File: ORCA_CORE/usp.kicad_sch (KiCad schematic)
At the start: 15 parts, among them U11 AP64502

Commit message: made usp (sketch only)
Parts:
- added C29: 0.01u, symbol Device:C
- added C30, C34, C35: 0.1u, symbol Device:C
- added C31, C32, C36, C37, C38, C41, C42, C43: 4.7u, symbol Device:C
- added C33: 1u, symbol Device:C
- added D15: LED_batt_enabled, symbol Device:LED_Filled
- added D16, D17, D18: CUHS20560, symbol Device:D_Schottky
- added L1: L, symbol Device:L
- added Q5: PMOS, symbol Simulation_SPICE:PMOS
- added R23, R24: 100k, symbol Device:R
- added R25: 47k, symbol Device:R
- added R26: 4.7k, symbol Device:R
- added R27: 510, symbol Device:R
- added R28, R32, R33: 10k, symbol Device:R
- added R29: 2k, symbol Device:R
- added R30: 100, symbol Device:R
- added R31: 1k, symbol Device:R
- added U12: TPS61230A__board, symbol mylib:TPS61230A_board
- U10: value ~ -> HY2112
- U9: value ~ -> FS8205
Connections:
- net GND: now also U11.7 (GND), U11.9 (PAD), U9.3, C29.2, C31.1, C32.1, C33.1, C34.1, C36.1, C37.1, C38.1, C41.1, C42.1, C43.1, D15.1 (K), R24.2, R28.2, R29.2, R32.2, U12.3 (GND), U12.5 (GND)
- net VDD: now also C24.1, R22.1, U3.4 (VIN), D17.2 (A), R32.1, R33.2; no longer U11.2 (Vin), U11.3 (EN)
- net bat+: now reaches C25.1, U3.5 (BAT), U3.8 (FB)
- net at U10.1 (OD): now also U9.6
- net at U10.2 (CS): now also R29.1
- net at U10.3 (OC): now also U9.4
- net at U10.5 (VDD): now also C35.1, R30.1
- net batt-: now reaches U10.6 (VSS)
- net batt-: now also U9.1, C35.2
- net at U11.1 (BST): now also C30.2
- net at U11.4 (RT/CLK): now also R23.1
- net at U11.5 (FB): now also R27.2, R28.1
- net at U11.6 (SS): now also C29.1
- net at U11.8 (SW): now also C30.1, L1.1
- new net: Q5.2 (G), R33.1
- new net: R23.2, R24.1
- new net: D15.2 (A), R31.2
- new net: R25.1, R26.1
- new net: R26.2, R27.1
- new net Vout: C31.2, C32.2, C33.2, C34.2, D16.1 (K), D18.1 (K)
- new net batt+: Q5.1 (D), R30.2
- new net reg_down: D17.1 (K), U11.2 (Vin), U11.3 (EN)
- new net reg_down_out: D18.2 (A), L1.2, R25.2
- new net reg_up: C36.2, C37.2, C38.2, Q5.3 (S), R31.1, U12.1 (VIN), U12.2 (EN)
- new net reg_up_out: C41.2, C42.2, C43.2, D16.2 (A), U12.4 (VOUT)
- no-connect marks 0 -> 3
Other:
- note added: "3.3V -> 5V2.5A DCDC"
- note added: "9V -> 5V3A DCDC"
- note added: "battery protection"
- note added: "charger"
- note added: "load sharing system"
- note added: "power"
- moved on the sheet: C24, C25, C26, C27, C28, D10, D12, D13, F2, R21, R22, U10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

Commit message: made all sketch for test (cpu board is only for test
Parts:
- removed F2: Polyfuse, symbol Device:Polyfuse
- added C39: 1000u, symbol Device:C_Polarized
- added F2: Fuse, symbol Device:Fuse
- D13: value D_Schottky -> CUHS20560
- L1: value L -> 10u
- Q5: value PMOS -> TJ60S04M3L
- U3: value ~ -> CN3058E
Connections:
- net GND: now also C39.1
- net Vin: now also F2.2
- net Vout: now also C39.2
- net VDD renamed VDD_usp
- net VDD_usp: now also F2.1; no longer D17.2 (A), R32.1, R33.2
- new net +VDD_power: D17.2 (A), R32.1, R33.2

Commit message: attach all capacitors
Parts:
- C24, C27, C33: footprint (none) -> Capacitor_SMD:C_0805_2012Metric_Pad1.18x1.45mm_HandSolder
- C25: footprint (none) -> Capacitor_SMD:C_1206_3216Metric_Pad1.33x1.80mm_HandSolder
- C26, C28, C30, C31, C32, C34, C35, C36, C37, C38, C41, C42, C43: footprint (none) -> Capacitor_SMD:C_0603_1608Metric_Pad1.08x0.95mm_HandSolder
- D10, D12, D15: footprint (none) -> LED_SMD:LED_0603_1608Metric_Pad1.05x0.95mm_HandSolder
- D13, D16, D17, D18: footprint (none) -> Diode:Diode_US2H
- L1: footprint (none) -> Inductor_SMD:L_12x12mm_H8mm
- Q5: footprint (none) -> toshiba:2-7M1A
- R21, R22, R23, R24, R25, R26, R27, R28, R29, R30, R31, R32, R33: footprint (none) -> Resistor_SMD:R_0603_1608Metric_Pad0.98x0.95mm_HandSolder

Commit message: attach all the footprints
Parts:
- C29: footprint (none) -> Capacitor_SMD:C_0603_1608Metric_Pad1.08x0.95mm_HandSolder
- C39: footprint (none) -> Capacitor_THT:CP_Radial_D10.0mm_P5.00mm
- U10, U9: footprint (none) -> Package_TO_SOT_SMD:TSOT-23-6_HandSoldering
- U12: footprint (none) -> Converter_DCDC:TPS61230A
- U3: footprint (none) -> Package_SO:TSSOP-8_3x3mm_P0.65mm
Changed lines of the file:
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@@
       (effects (font (size 1.27 1.27)))
     )
-    (property "Footprint" "" (at 69.85 99.06 0)
+    (property "Footprint" "Package_SO:TSSOP-8_3x3mm_P0.65mm" (at 69.85 99.06 0)
       (effects (font (size 1.27 1.27)) hide)
     )
@@
       (effects (font (size 1.27 1.27)))
     )
-    (property "Footprint" "" (at 195.58 87.63 0)
+    (property "Footprint" "Package_TO_SOT_SMD:TSOT-23-6_HandSoldering" (at 195.58 87.63 0)
       (effects (font (size 1.27 1.27)) hide)
     )
@@
       (effects (font (size 1.27 1.27)) (justify left))
     )
-    (property "Footprint" "" (at 116.5352 49.53 0)
+    (property "Footprint" "Capacitor_SMD:C_0603_1608Metric_Pad1.08x0.95mm_HandSolder" (at 116.5352 49.53 0)
       (effects (font (size 1.27 1.27)) hide)
     )
@@
       (effects (font (size 1.27 1.27)))
     )
-    (property "Footprint" "" (at 195.58 101.6 0)
+    (property "Footprint" "Package_TO_SOT_SMD:TSOT-23-6_HandSoldering" (at 195.58 101.6 0)
       (effects (font (size 1.27 1.27)) hide)
     )
@@
       (effects (font (size 1.27 1.27)) (justify left))
     )
-    (property "Footprint" "" (at 153.3652 152.4 0)
+    (property "Footprint" "Capacitor_THT:CP_Radial_D10.0mm_P5.00mm" (at 153.3652 152.4 0)
       (effects (font (size 1.27 1.27)) hide)
     )
@@
       (effects (font (size 1.27 1.27)))
     )
-    (property "Footprint" "" (at 246.38 34.29 0)
-      (effects (font (size 1.27 1.27)) hide)
-    )
+    (property "Footprint" "Converter_DCDC:TPS61230A" (at 246.38 34.29 0)
+      (effects (font (size 1.27 1.27)) hide)
+    )

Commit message: change sketch a little
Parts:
- F2: footprint (none) -> fuse:fuse
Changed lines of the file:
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@@
       (effects (font (size 1.27 1.27)))
     )
-    (property "Footprint" "" (at 35.56 28.702 90)
+    (property "Footprint" "fuse:fuse" (at 35.56 28.702 90)
       (effects (font (size 1.27 1.27)) hide)
     )

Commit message: plate power
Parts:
- added H5, H6, H7, H8: Hole_usp, MountingHole:MountingHole_3.2mm_M3, symbol Mechanical:MountingHole
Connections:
- net VDD_usp is gone; now on net +VDD_usp: C24.1, C26.2, C27.2, C28.2, D13.1 (K), F2.1, R22.1, U3.4 (VIN)
- net +VDD_power renamed +VDD_usp
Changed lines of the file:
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@@
     )
   )
-  (global_label "+VDD_power" (shape input) (at 35.56 171.45 180) (fields_autoplaced)
+  (global_label "+VDD_usp" (shape input) (at 35.56 171.45 180) (fields_autoplaced)
     (effects (font (size 1.27 1.27)) (justify right))
-    (property "Intersheetrefs" "${INTERSHEET_REFS}" (at 20.9029 171.45 0)
+    (property "Intersheetrefs" "${INTERSHEET_REFS}" (at 23.0801 171.45 0)
       (effects (font (size 1.27 1.27)) (justify right) hide)
     )
@@
     )
   )
-  (global_label "VDD_usp" (shape input) (at 190.5 168.91 180) (fields_autoplaced)
+  (global_label "+VDD_usp" (shape input) (at 190.5 168.91 180) (fields_autoplaced)
     (effects (font (size 1.27 1.27)) (justify right))
-    (property "Intersheetrefs" "${INTERSHEET_REFS}" (at 179.5925 168.91 0)
+    (property "Intersheetrefs" "${INTERSHEET_REFS}" (at 178.0201 168.91 0)
       (effects (font (size 1.27 1.27)) (justify right) hide)
     )
@@
     )
   )
-  (global_label "VDD_usp" (shape input) (at 73.66 30.48 0) (fields_autoplaced)
+  (global_label "+VDD_usp" (shape input) (at 73.66 30.48 0) (fields_autoplaced)
     (effects (font (size 1.27 1.27)) (justify left))
-    (property "Intersheetrefs" "${INTERSHEET_REFS}" (at 84.5675 30.48 0)
+    (property "Intersheetrefs" "${INTERSHEET_REFS}" (at 86.1399 30.48 0)
       (effects (font (size 1.27 1.27)) (justify left) hide)
     )
@@
     )
   )
-  (global_label "VDD_usp" (shape input) (at 46.99 74.93 180) (fields_autoplaced)
+  (global_label "+VDD_usp" (shape input) (at 46.99 74.93 180) (fields_autoplaced)
     (effects (font (size 1.27 1.27)) (justify right))
-    (property "Intersheetrefs" "${INTERSHEET_REFS}" (at 36.0825 74.93 0)
+    (property "Intersheetrefs" "${INTERSHEET_REFS}" (at 34.5101 74.93 0)
       (effects (font (size 1.27 1.27)) (justify right) hide)
     )
@@
         (path "/895d6bb7-4008-488b-a34b-0077e9f7e4a1/6a7faaf2-e424-4dfa-bbc5-1df218d33dea"
           (reference "#PWR062") (unit 1)
+        )
+      )
+    )
+  )
+  (symbol (lib_id "Mechanical:MountingHole") (at 246.38 177.8 0) (unit 1)
+    (in_bom yes) (on_board yes) (dnp no) (fields_autoplaced)
+    (property "Reference" "H6" (at 248.92 176.53 0)
+      (effects (font (size 1.27 1.27)) (justify left))
+    )
+    (property "Value" "Hole_usp" (at 248.92 179.07 0)
+      (effects (font (size 1.27 1.27)) (justify left))
+    )
+    (property "Footprint" "MountingHole:MountingHole_3.2mm_M3" (at 246.38 177.8 0)
+      (effects (font (size 1.27 1.27)) hide)
+    )
+    (property "Datasheet" "~" (at 246.38 177.8 0)
+      (effects (font (size 1.27 1.27)) hide)
+    )
+    (instances
+      (project "ORCA_CORE"
+        (path "/895d6bb7-4008-488b-a34b-0077e9f7e4a1/6a7faaf2-e424-4dfa-bbc5-1df218d33dea"
+          (reference "H6") (unit 1)
         )
       )
@@
     )
   )
+  (symbol (lib_id "Mechanical:MountingHole") (at 264.16 170.18 0) (unit 1)
+    (in_bom yes) (on_board yes) (dnp no) (fields_autoplaced)
+    (property "Reference" "H7" (at 266.7 168.91 0)
+      (effects (font (size 1.27 1.27)) (justify left))
+    )
+    (property "Value" "Hole_usp" (at 266.7 171.45 0)
+      (effects (font (size 1.27 1.27)) (justify left))
+    )
+    (property "Footprint" "MountingHole:MountingHole_3.2mm_M3" (at 264.16 170.18 0)
+      (effects (font (size 1.27 1.27)) hide)
+    )
+    (property "Datasheet" "~" (at 264.16 170.18 0)
+      (effects (font (size 1.27 1.27)) hide)
+    )
+    (instances
+      (project "ORCA_CORE"
+        (path "/895d6bb7-4008-488b-a34b-0077e9f7e4a1/6a7faaf2-e424-4dfa-bbc5-1df218d33dea"
+          (reference "H7") (unit 1)
+        )
+      )
+    )
+  )
   (symbol (lib_id "Device:D_Schottky") (at 105.41 152.4 180) (unit 1)
     (in_bom yes) (on_board yes) (dnp no) (fields_autoplaced)
@@
     )
   )
+  (symbol (lib_id "Mechanical:MountingHole") (at 246.38 170.18 0) (unit 1)
+    (in_bom yes) (on_board yes) (dnp no) (fields_autoplaced)
+    (property "Reference" "H5" (at 248.92 168.91 0)
+      (effects (font (size 1.27 1.27)) (justify left))
+    )
+    (property "Value" "Hole_usp" (at 248.92 171.45 0)
+      (effects (font (size 1.27 1.27)) (justify left))
+    )
+    (property "Footprint" "MountingHole:MountingHole_3.2mm_M3" (at 246.38 170.18 0)
+      (effects (font (size 1.27 1.27)) hide)
+    )
+    (property "Datasheet" "~" (at 246.38 170.18 0)
+      (effects (font (size 1.27 1.27)) hide)
+    )
+    (instances
+      (project "ORCA_CORE"
+        (path "/895d6bb7-4008-488b-a34b-0077e9f7e4a1/6a7faaf2-e424-4dfa-bbc5-1df218d33dea"
+          (reference "H5") (unit 1)
+        )
+      )
+    )
+  )
   (symbol (lib_id "Device:R") (at 95.25 80.01 0) (unit 1)
     (in_bom yes) (on_board yes) (dnp no) (fields_autoplaced)
@@
         )
       )
+    )
+  )
+  (symbol (lib_id "Mechanical:MountingHole") (at 264.16 177.8 0) (unit 1)
+    (in_bom yes) (on_board yes) (dnp no) (fields_autoplaced)
+    (property "Reference" "H8" (at 266.7 176.53 0)
+      (effects (font (size 1.27 1.27)) (justify left))
+    )
+    (property "Value" "Hole_usp" (at 266.7 179.07 0)
+      (effects (font (size 1.27 1.27)) (justify left))
+    )
+    (property "Footprint" "MountingHole:MountingHole_3.2mm_M3" (at 264.16 177.8 0)
+      (effects (font (size 1.27 1.27)) hide)
+    )
+    (property "Datasheet" "~" (at 264.16 177.8 0)
+      (effects (font (size 1.27 1.27)) hide)
+    )
+    (instances
+      (project "ORCA_CORE"
+        (path "/895d6bb7-4008-488b-a34b-0077e9f7e4a1/6a7faaf2-e424-4dfa-bbc5-1df218d33dea"
+          (reference "H8") (unit 1)
+        )
+      )

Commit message: plate power and usp
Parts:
- removed H7, H8: Hole_usp, MountingHole:MountingHole_3.2mm_M3, symbol Mechanical:MountingHole
- added C51: 4.7u, Capacitor_SMD:C_0603_1608Metric_Pad1.08x0.95mm_HandSolder, symbol Device:C
- added J21: Conn_01x02, Battery:BatteryHolder_1xAA_code, symbol Connector_Generic:Conn_01x02
- added R5: 0, Resistor_SMD:R_0603_1608Metric_Pad0.98x0.95mm_HandSolder, symbol Device:R
- L1: footprint Inductor_SMD:L_12x12mm_H8mm -> Inductor_SMD:L_12x12mm_H8mm_withmodel
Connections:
- net bat+ is gone; now on net batt+: C25.1, U3.5 (BAT), U3.8 (FB)
- net GND: now also C51.1, R5.1; no longer C31.1, C32.1, C33.1, C34.1, C39.1
- net batt+: now also J21.2 (Pin_2)
- net batt-: now also J21.1 (Pin_1)
- net reg_down: now also C41.2, C42.2, C43.2, D18.1 (K), C51.2
- net reg_down_out: now also C31.2, C32.2, C33.2, C34.2, C39.1, D16.1 (K)
- net reg_up_out: no longer C41.2, C42.2, C43.2
- removed net Vout: C31.2, C32.2, C33.2, C34.2, C39.2, D16.1 (K), D18.1 (K)
- new net GND1: C31.1, C32.1, C33.1, C34.1, C39.2, R5.2
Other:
- moved on the sheet: C29, C30, C35, C39, C41, C42, C43, D18, L1, R23, R24, R25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

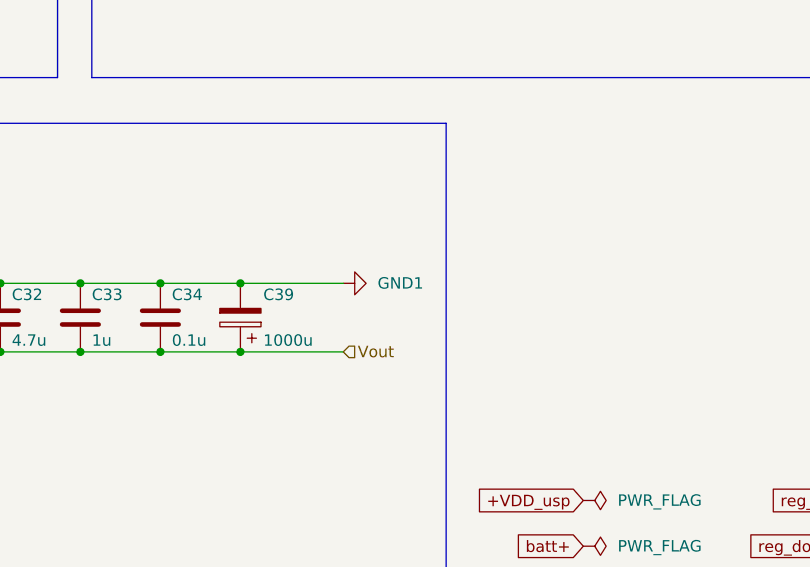
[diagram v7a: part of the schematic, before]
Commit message: complete wireing and filling usp
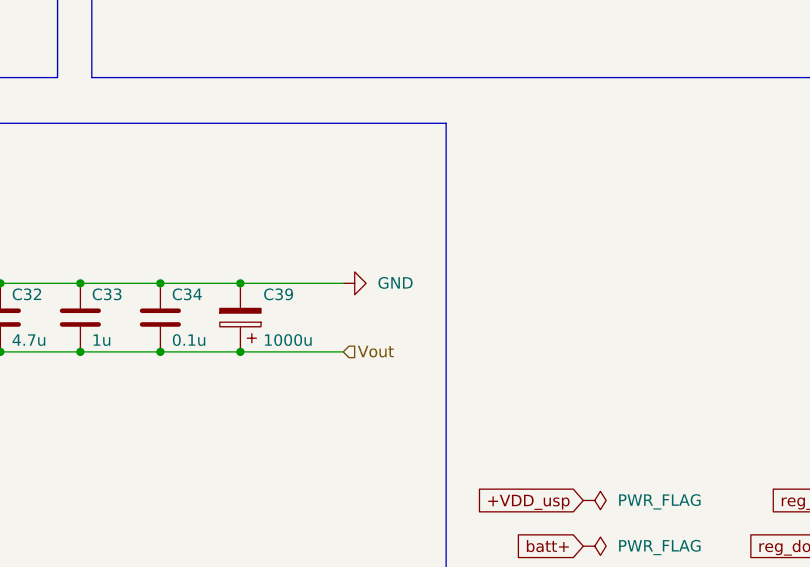
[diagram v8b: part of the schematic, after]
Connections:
- net GND: now also C31.1, C32.1, C33.1, C34.1, C39.2
- net GND1: no longer C31.1, C32.1, C33.1, C34.1, C39.2
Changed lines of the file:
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@@
+    )
+  )
+  (symbol (lib_id "power:GND") (at 163.83 144.78 90) (unit 1)
+    (in_bom yes) (on_board yes) (dnp no) (fields_autoplaced)
+    (property "Reference" "#PWR010" (at 170.18 144.78 0)
+      (effects (font (size 1.27 1.27)) hide)
+    )
+    (property "Value" "GND" (at 167.64 144.78 90)
+      (effects (font (size 1.27 1.27)) (justify right))
+    )
+    (property "Footprint" "" (at 163.83 144.78 0)
+      (effects (font (size 1.27 1.27)) hide)
+    )
+    (property "Datasheet" "" (at 163.83 144.78 0)
+      (effects (font (size 1.27 1.27)) hide)
+    )
+    (pin "1")
+    (instances
+      (project "ORCA_CORE"
+        (path "/895d6bb7-4008-488b-a34b-0077e9f7e4a1/6a7faaf2-e424-4dfa-bbc5-1df218d33dea"
+          (reference "#PWR010") (unit 1)
+        )
+      )
     )
   )
@@
         )
       )
-    )
-  )
-  (symbol (lib_id "power:GND1") (at 163.83 144.78 90) (unit 1)
-    (in_bom yes) (on_board yes) (dnp no) (fields_autoplaced)
-    (property "Reference" "#PWR010" (at 170.18 144.78 0)
-      (effects (font (size 1.27 1.27)) hide)
-    )
-    (property "Value" "GND1" (at 167.64 144.78 90)
-      (effects (font (size 1.27 1.27)) (justify right))
-    )
-    (property "Footprint" "" (at 163.83 144.78 0)
-      (effects (font (size 1.27 1.27)) hide)
-    )
-    (property "Datasheet" "" (at 163.83 144.78 0)
-      (effects (font (size 1.27 1.27)) hide)
-    )
-    (pin "1")
-    (instances
-      (project "ORCA_CORE"
-        (path "/895d6bb7-4008-488b-a34b-0077e9f7e4a1/6a7faaf2-e424-4dfa-bbc5-1df218d33dea"
-          (reference "#PWR010") (unit 1)
-        )
-      )
